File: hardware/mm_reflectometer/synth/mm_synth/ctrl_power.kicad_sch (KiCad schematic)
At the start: 60 parts

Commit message: library updates
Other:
- note added: "CHANGE TO DBVR PACKAGE"
- note added: "CHANGE TO DCKR PACKAGE"
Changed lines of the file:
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@@
     (effects (font (size 1.27 1.27)) (justify left bottom))
+  )
+  (text "CHANGE TO DBVR PACKAGE" (at 334.01 187.96 180)
+    (effects (font (size 3 3) (thickness 0.6) bold) (justify right bottom))
+  )
+  (text "CHANGE TO DCKR PACKAGE" (at 334.645 92.075 180)
+    (effects (font (size 3 3) (thickness 0.6) bold) (justify right bottom))
   )
   (label "PGOOD" (at 264.795 59.055 0)

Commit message: adding digital connections to synth schematic
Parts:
- removed C? (x4): 1uF, Capacitor_SMD:C_0402_1005Metric, symbol Device:C
- removed C? (x4): 10uF, Capacitor_SMD:C_0603_1608Metric, symbol Device:C
- removed C? (x3): 4.7uF, Capacitor_SMD:C_0402_1005Metric, symbol Device:C
- removed C? (x2): 6.8pF, Capacitor_SMD:C_0402_1005Metric, symbol Device:C
- removed R?: 10k, Resistors_SMD:R_0402, symbol Device:R_Small
- removed R?: 10k, Resistor_SMD:R_0402_1005Metric, symbol Device:R
- removed R?: 47k, Resistor_SMD:R_0402_1005Metric, symbol Device:R
- removed R?: 210k, Resistor_SMD:R_0402_1005Metric, symbol Device:R
- removed R?: 100k, Resistor_SMD:R_0402_1005Metric, symbol Device:R
- removed R?: 24k3, Resistor_SMD:R_0402_1005Metric, symbol Device:R
- removed R?: 84k5, Resistor_SMD:R_0402_1005Metric, symbol Device:R
- added C? (x7): 10 uF, Capacitors_SMD:C_0603, symbol Device:C_Small
- added C? (x4): 2.2 uF, Capacitors_SMD:C_0603, symbol Device:C_Small
- added C? (x2): 6.8 pF, symbol Device:C_Small
- added R?: 10k, Resistor_SMD:R_0402_1005Metric, symbol Device:R_Small
- added R?: 210k, symbol Device:R_Small
- added R? (x2): 10k, Resistors_SMD:R_0402, symbol Device:R_Small
- added R?: 100k, symbol Device:R_Small
- added R?: 47k, symbol Device:R_Small
- added R?: 84.5k, symbol Device:R_Small
- R? (x2): value 10k -> DNI
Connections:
- net PGOOD_5V5 is gone; now on net PGOOD_SWITCHING: U?.B4 (PGOOD2)
- net +1V1: now also C?.1, C?.1, C?.1, R?.1
- net +1V8: now also C?.1, C?.1
- net +2V5: now also C?.1, C?.1
- net +3V3: now also C?.1, C?.1, C?.1, C?.1, R?.1
- net +4V: now also R?.2; no longer C?.1, L?.1
- net +5V: now also C?.1, C?.1
- net +9V: now also C?.1, L?.1, R?.2, R?.2
- net GND: now also C?.2, C?.2, C?.2, C?.2, C?.2, C?.2, C?.2, C?.2, C?.2, C?.2, C?.2, R?.2, R?.2, R?.2
- net at U?.1 (FB): now also C?.2, R?.1, R?.2 (x2)
- net 4V0_EN: no longer names the net of R?.1, U?.D2 (RUN1)
- net 4V0_EN: now also R?.1
- net 5V5_EN: no longer names the net of R?.1, U?.B2 (RUN2)
- net 5V5_EN: now also R?.1
- net PGOOD renamed DIGITAL_SEQ_EN
- net DIGITAL_SEQ_EN: now also R?.1
- net PGOOD_4V0 renamed PGOOD_SWITCHING
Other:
- note added: "9V +/- 10% input, TBD A"
- note added: "CHANGE SERIES INDUCTOR"
- note added: "SET NEW OV/UV RESISTORS"
- note removed: "4V +/- 5% input, 1.5A"
- note removed: "TBD PULLUP ON PGOOD"
- note removed: "USB PD?"
- moved on the sheet: L?, R?, U?

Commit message: work on mm synth schematic - control signals and footprint assignments
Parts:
- removed L?: BLM18EG101TN1D, Inductor_SMD:L_0603_1608Metric, symbol Device:L_Small
- added FB?: BLM18EG101TN1D, symbol Device:FerriteBead_Small
- C1502, C1506, C1510, C1511, C1513, C1514, C1515, C1516, C1517, C1520, C1521, C1522, C1523, C1524, C1525: renamed from C?; footprint Capacitors_SMD:C_0603 -> Capacitor_SMD:C_0603_1608Metric
- C1504, C1505: renamed from C?; footprint Capacitors_SMD:C_0402 -> Capacitor_SMD:C_0402_1005Metric
- C1507, C1508: renamed from C?; footprint Capacitors_SMD:C_1210 -> Capacitor_SMD:C_1210_3225Metric
- C1518, C1519: renamed from C?; footprint (none) -> Capacitor_SMD:C_0402_1005Metric
- R1519, R1520, R1521, R1522: renamed from R?; footprint (none) -> Resistor_SMD:R_0402_1005Metric
- gave numbers to parts that had none: 33
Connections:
- net +9V: now also FB?.2
- net at C1509.1, Q1501.5 (D2), Q1501.6 (D2)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: now also FB?.1
- net ~FPGA_RESET renamed ~{FPGA_RESET}

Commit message: added aux high speed io connector, fixed hierarchical buses
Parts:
- FB1501: renamed from FB?; footprint (none) -> Inductor_SMD:L_0603_1608Metric
- R1501, R1502, R1503, R1504, R1508, R1509, R1511, R1513, R1514: footprint Resistors_SMD:R_0402 -> Resistor_SMD:R_0402_1005Metric
- renumbered L1502 to L1501, L1503 to L1502
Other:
- note added: "VERIFY SEQUENCING"
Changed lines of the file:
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@@
     (effects (font (size 1.27 1.27)) (justify left bottom))
+  )
+  (text "VERIFY SEQUENCING\n" (at 242.57 26.67 0)
+    (effects (font (size 3 3) (thickness 0.6) bold) (justify left bottom))
   )
   (text "Turn on at VBUS >4.1V" (at 279.4 69.85 0)
@@
   (symbol (lib_id "Device:L_Small") (at 308.61 148.59 90) (unit 1)
     (in_bom yes) (on_board yes)
-    (property "Reference" "L1502" (id 0) (at 308.61 143.9988 90))
+    (property "Reference" "L1501" (id 0) (at 308.61 143.9988 90))
     (property "Value" "2.2uH" (id 1) (at 308.61 146.2975 90))
     (property "Footprint" "Inductor_SMD:L_0805_2012Metric" (id 2) (at 308.61 148.59 0)
@@
   (symbol (lib_id "Device:L_Small") (at 308.61 195.58 90) (unit 1)
     (in_bom yes) (on_board yes)
-    (property "Reference" "L1503" (id 0) (at 308.61 190.9888 90))
+    (property "Reference" "L1502" (id 0) (at 308.61 190.9888 90))
     (property "Value" "2.2uH" (id 1) (at 308.61 193.2875 90))
     (property "Footprint" "Inductor_SMD:L_0805_2012Metric" (id 2) (at 308.61 195.58 0)
@@
       (effects (font (size 1.27 1.27)) (justify left))
     )
-    (property "Footprint" "Resistors_SMD:R_0402" (id 2) (at 83.82 175.26 0)
+    (property "Footprint" "Resistor_SMD:R_0402_1005Metric" (id 2) (at 83.82 175.26 0)
       (effects (font (size 1.27 1.27)) hide)
     )
@@
       (effects (font (size 1.27 1.27)) (justify left))
     )
-    (property "Footprint" "Resistors_SMD:R_0402" (id 2) (at 83.82 189.23 0)
+    (property "Footprint" "Resistor_SMD:R_0402_1005Metric" (id 2) (at 83.82 189.23 0)
       (effects (font (size 1.27 1.27)) hide)
     )
@@
       (effects (font (size 1.27 1.27)) (justify left))
     )
-    (property "Footprint" "Resistors_SMD:R_0402" (id 2) (at 90.17 175.26 0)
+    (property "Footprint" "Resistor_SMD:R_0402_1005Metric" (id 2) (at 90.17 175.26 0)
       (effects (font (size 1.27 1.27)) hide)
     )
@@
       (effects (font (size 1.27 1.27)) (justify left))
     )
-    (property "Footprint" "Resistors_SMD:R_0402" (id 2) (at 90.17 189.23 0)
+    (property "Footprint" "Resistor_SMD:R_0402_1005Metric" (id 2) (at 90.17 189.23 0)
       (effects (font (size 1.27 1.27)) hide)
     )
@@
       (effects (font (size 1.27 1.27)) (justify left))
     )
-    (property "Footprint" "Resistors_SMD:R_0402" (id 2) (at 105.41 187.96 0)
+    (property "Footprint" "Resistor_SMD:R_0402_1005Metric" (id 2) (at 105.41 187.96 0)
       (effects (font (size 1.27 1.27)) hide)
     )
@@
       (effects (font (size 1.27 1.27)) (justify left))
     )
-    (property "Footprint" "Resistors_SMD:R_0402" (id 2) (at 110.49 209.55 0)
+    (property "Footprint" "Resistor_SMD:R_0402_1005Metric" (id 2) (at 110.49 209.55 0)
       (effects (font (size 1.27 1.27)) hide)
     )
@@
       (effects (font (size 1.27 1.27)) (justify left))
     )
-    (property "Footprint" "Resistors_SMD:R_0402" (id 2) (at 128.27 134.62 0)
+    (property "Footprint" "Resistor_SMD:R_0402_1005Metric" (id 2) (at 128.27 134.62 0)
       (effects (font (size 1.27 1.27)) hide)
     )
@@
       (effects (font (size 1.27 1.27)) (justify left))
     )
-    (property "Footprint" "Resistors_SMD:R_0402" (id 2) (at 152.4 200.66 0)
+    (property "Footprint" "Resistor_SMD:R_0402_1005Metric" (id 2) (at 152.4 200.66 0)
       (effects (font (size 1.27 1.27)) hide)
     )
@@
       (effects (font (size 1.27 1.27)) (justify left))
     )
-    (property "Footprint" "Resistors_SMD:R_0402" (id 2) (at 161.29 200.66 0)
+    (property "Footprint" "Resistor_SMD:R_0402_1005Metric" (id 2) (at 161.29 200.66 0)
       (effects (font (size 1.27 1.27)) hide)
     )
@@
   (symbol (lib_id "Device:FerriteBead_Small") (at 168.91 41.91 90) (unit 1)
     (in_bom yes) (on_board yes)
-    (property "Reference" "FB?" (id 0) (at 163.83 44.45 90))
+    (property "Reference" "FB1501" (id 0) (at 163.83 44.45 90))
     (property "Value" "BLM18EG101TN1D" (id 1) (at 168.91 46.99 90))
-    (property "Footprint" "" (id 2) (at 168.91 43.688 90)
-      (effects (font (size 1.27 1.27)) hide)
-    )
+    (property "Footprint" "Inductor_SMD:L_0603_1608Metric" (id 2) (at 168.91 43.688 90)
+      (effects (font (size 1.27 1.27)) hide)
+    )

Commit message: schematic cleanup, erc
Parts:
- C1501: symbol vna_mm_ref-rescue:CP1-Device -> Device:C_Polarized_Small
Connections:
- net +4V: now also C1514.1, C1515.1, U1505.3 (VIN), U1506.3 (VIN)
- net +5V: no longer C1514.1, C1515.1, U1505.3 (VIN), U1506.3 (VIN)
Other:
- note added: "ADD INPUT POWER CONNECTFOR ADD +5V REGULATOR"
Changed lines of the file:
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@@
   (no_connect (at 149.86 179.07))
   (no_connect (at 149.86 181.61))
-  (wire (pts (xy 73.66 35.56) (xy 73.66 48.26))
-    (stroke (width 0) (type solid) (color 0 0 0 0))
-  )
-  (wire (pts (xy 73.66 55.88) (xy 73.66 58.42))
+  (wire (pts (xy 73.66 35.56) (xy 73.66 49.53))
+    (stroke (width 0) (type solid) (color 0 0 0 0))
+  )
+  (wire (pts (xy 73.66 54.61) (xy 73.66 58.42))
     (stroke (width 0) (type solid) (color 0 0 0 0))
   )
@@
   (text "SET NEW OV/UV RESISTORS" (at 31.75 73.66 0)
     (effects (font (size 3 3) (thickness 0.6) bold) (justify left bottom))
+  )
+  (text "ADD INPUT POWER CONNECTFOR\nADD +5V REGULATOR" (at 73.66 116.84 0)
+    (effects (font (size 5 5) (thickness 1) bold) (justify left bottom))
   )
   (text "9V +/- 10% input, TBD A" (at 80.01 26.67 0)
@@
     (pin "1")
   )
+  (symbol (lib_id "power:+4V") (at 278.13 148.59 0) (unit 1)
+    (in_bom yes) (on_board yes)
+    (property "Reference" "#PWR0102" (id 0) (at 278.13 152.4 0)
+      (effects (font (size 1.27 1.27)) hide)
+    )
+    (property "Value" "+4V" (id 1) (at 275.59 144.3354 0)
+      (effects (font (size 1.27 1.27)) (justify left))
+    )
+    (property "Footprint" "" (id 2) (at 278.13 148.59 0)
+      (effects (font (size 1.27 1.27)) hide)
+    )
+    (property "Datasheet" "" (id 3) (at 278.13 148.59 0)
+      (effects (font (size 1.27 1.27)) hide)
+    )
+    (pin "1")
+  )
+  (symbol (lib_id "power:+4V") (at 278.13 195.58 0) (unit 1)
+    (in_bom yes) (on_board yes)
+    (property "Reference" "#PWR0101" (id 0) (at 278.13 199.39 0)
+      (effects (font (size 1.27 1.27)) hide)
+    )
+    (property "Value" "+4V" (id 1) (at 275.59 191.3254 0)
+      (effects (font (size 1.27 1.27)) (justify left))
+    )
+    (property "Footprint" "" (id 2) (at 278.13 195.58 0)
+      (effects (font (size 1.27 1.27)) hide)
+    )
+    (property "Datasheet" "" (id 3) (at 278.13 195.58 0)
+      (effects (font (size 1.27 1.27)) hide)
+    )
+    (pin "1")
+  )
   (symbol (lib_id "power:+5V") (at 295.91 44.45 0) (unit 1)
     (in_bom yes) (on_board yes)
@@
     (pin "")
   )
-  (symbol (lib_id "gkl_power:GND") (at 313.69 173.99 0) (unit 1)
-    (in_bom yes) (on_board yes)
-    (property "Reference" "#PWR01550" (id 0) (at 313.69 180.34 0)
-      (effects (font (size 1.27 1.27)) hide)
-    )
-    (property "Value" "GND" (id 1) (at 313.7662 177.1904 0))
-    (property "Footprint" "" (id 2) (at 311.15 182.88 0)
-      (effects (font (size 1.27 1.27)) hide)
-    )
-    (property "Datasheet" "" (id 3) (at 313.69 173.99 0)
-      (effects (font (size 1.27 1.27)) hide)
-    )
-    (pin "1")
-  )
   (symbol (lib_id "Device:L_Small") (at 308.61 148.59 90) (unit 1)
     (in_bom yes) (on_board yes)
@@
     (pin "2")
   )
-  (symbol (lib_id "gkl_power:+5V") (at 278.13 148.59 0) (unit 1)
-    (in_bom yes) (on_board yes)
-    (property "Reference" "#PWR01539" (id 0) (at 278.13 152.4 0)
-      (effects (font (size 1.27 1.27)) hide)
-    )
-    (property "Value" "+5V" (id 1) (at 278.2062 144.7546 0))
-    (property "Footprint" "" (id 2) (at 278.13 148.59 0)
-      (effects (font (size 1.27 1.27)) hide)
-    )
-    (property "Datasheet" "" (id 3) (at 278.13 148.59 0)
-      (effects (font (size 1.27 1.27)) hide)
-    )
-    (pin "1")
-  )
-  (symbol (lib_id "gkl_power:+5V") (at 278.13 195.58 0) (unit 1)
-    (in_bom yes) (on_board yes)
-    (property "Reference" "#PWR01541" (id 0) (at 278.13 199.39 0)
-      (effects (font (size 1.27 1.27)) hide)
-    )
-    (property "Value" "+5V" (id 1) (at 278.2062 191.7446 0))
-    (property "Footprint" "" (id 2) (at 278.13 195.58 0)
-      (effects (font (size 1.27 1.27)) hide)
-    )
-    (property "Datasheet" "" (id 3) (at 278.13 195.58 0)
-      (effects (font (size 1.27 1.27)) hide)
-    )
-    (pin "1")
-  )
   (symbol (lib_id "power:GND") (at 73.66 58.42 0) (unit 1)
     (in_bom yes) (on_board yes)
@@
     )
     (property "Datasheet" "" (id 3) (at 307.34 115.57 0)
+      (effects (font (size 1.27 1.27)) hide)
+    )
+    (pin "1")
+  )
+  (symbol (lib_id "power:GND") (at 313.69 173.99 0) (unit 1)
+    (in_bom yes) (on_board yes)
+    (property "Reference" "#PWR0103" (id 0) (at 313.69 180.34 0)
+      (effects (font (size 1.27 1.27)) hide)
+    )
+    (property "Value" "GND" (id 1) (at 313.69 177.8 0))
+    (property "Footprint" "" (id 2) (at 313.69 173.99 0)
+      (effects (font (size 1.27 1.27)) hide)
+    )
+    (property "Datasheet" "" (id 3) (at 313.69 173.99 0)
       (effects (font (size 1.27 1.27)) hide)
     )
@@
     (pin "2")
   )
+  (symbol (lib_id "Device:C_Polarized_Small") (at 73.66 52.07 0) (unit 1)
+    (in_bom yes) (on_board yes)
+    (property "Reference" "C1501" (id 0) (at 76.581 50.9016 0)
+      (effects (font (size 1.27 1.27)) (justify left))
+    )
+    (property "Value" "330 uF" (id 1) (at 76.581 53.213 0)
+      (effects (font (size 1.27 1.27)) (justify left))
+    )
+    (property "Footprint" "Capacitor_SMD:CP_Elec_6.3x5.9" (id 2) (at 73.66 52.07 0)
+      (effects (font (size 1.27 1.27)) hide)
+    )
+    (property "Datasheet" "~" (id 3) (at 73.66 52.07 0)
+      (effects (font (size 1.27 1.27)) hide)
+    )
+    (property "MAN_NAME" "Panasonic" (id 4) (at 73.66 52.07 0)
+      (effects (font (size 1.27 1.27)) hide)
+    )
+    (property "MAN_PN" "6SVPC330M" (id 5) (at 73.66 52.07 0)
+      (effects (font (size 1.27 1.27)) hide)
+    )
+    (property "DIST_NAME" "Digi-Key" (id 6) (at 73.66 52.07 0)
+      (effects (font (size 1.27 1.27)) hide)
+    )
+    (property "DIST_PN" "P16611CT-ND" (id 7) (at 73.66 52.07 0)
+      (effects (font (size 1.27 1.27)) hide)
+    )
+    (pin "1")
+    (pin "2")
+  )
   (symbol (lib_id "Device:C_Small") (at 87.63 153.67 0) (unit 1)
     (in_bom yes) (on_board yes)
@@
       (effects (font (size 1.27 1.27)) hide)
     )
-    (pin "1")
-    (pin "2")
-  )
-  (symbol (lib_id "vna_mm_ref-rescue:CP1-Device") (at 73.66 52.07 0) (unit 1)
-    (in_bom yes) (on_board yes)
-    (property "Reference" "C1501" (id 0) (at 76.581 50.9016 0)
-      (effects (font (size 1.27 1.27)) (justify left))
-    )
-    (property "Value" "330 uF" (id 1) (at 76.581 53.213 0)
-      (effects (font (size 1.27 1.27)) (justify left))
-    )
-    (property "Footprint" "Capacitor_SMD:CP_Elec_6.3x5.9" (id 2) (at 73.66 52.07 0)
-      (effects (font (size 1.27 1.27)) hide)
-    )
-    (property "Datasheet" "~" (id 3) (at 73.66 52.07 0)
-      (effects (font (size 1.27 1.27)) hide)
-    )
-    (property "MAN_NAME" "Panasonic" (id 4) (at 73.66 52.07 0)
-      (effects (font (size 1.27 1.27)) hide)
-    )
-    (property "MAN_PN" "6SVPC330M" (id 5) (at 73.66 52.07 0)
-      (effects (font (size 1.27 1.27)) hide)
-    )
-    (property "DIST_NAME" "Digi-Key" (id 6) (at 73.66 52.07 0)
-      (effects (font (size 1.27 1.27)) hide)
-    )
-    (property "DIST_PN" "P16611CT-ND" (id 7) (at 73.66 52.07 0)
-      (effects (font (size 1.27 1.27)) hide)
-    )

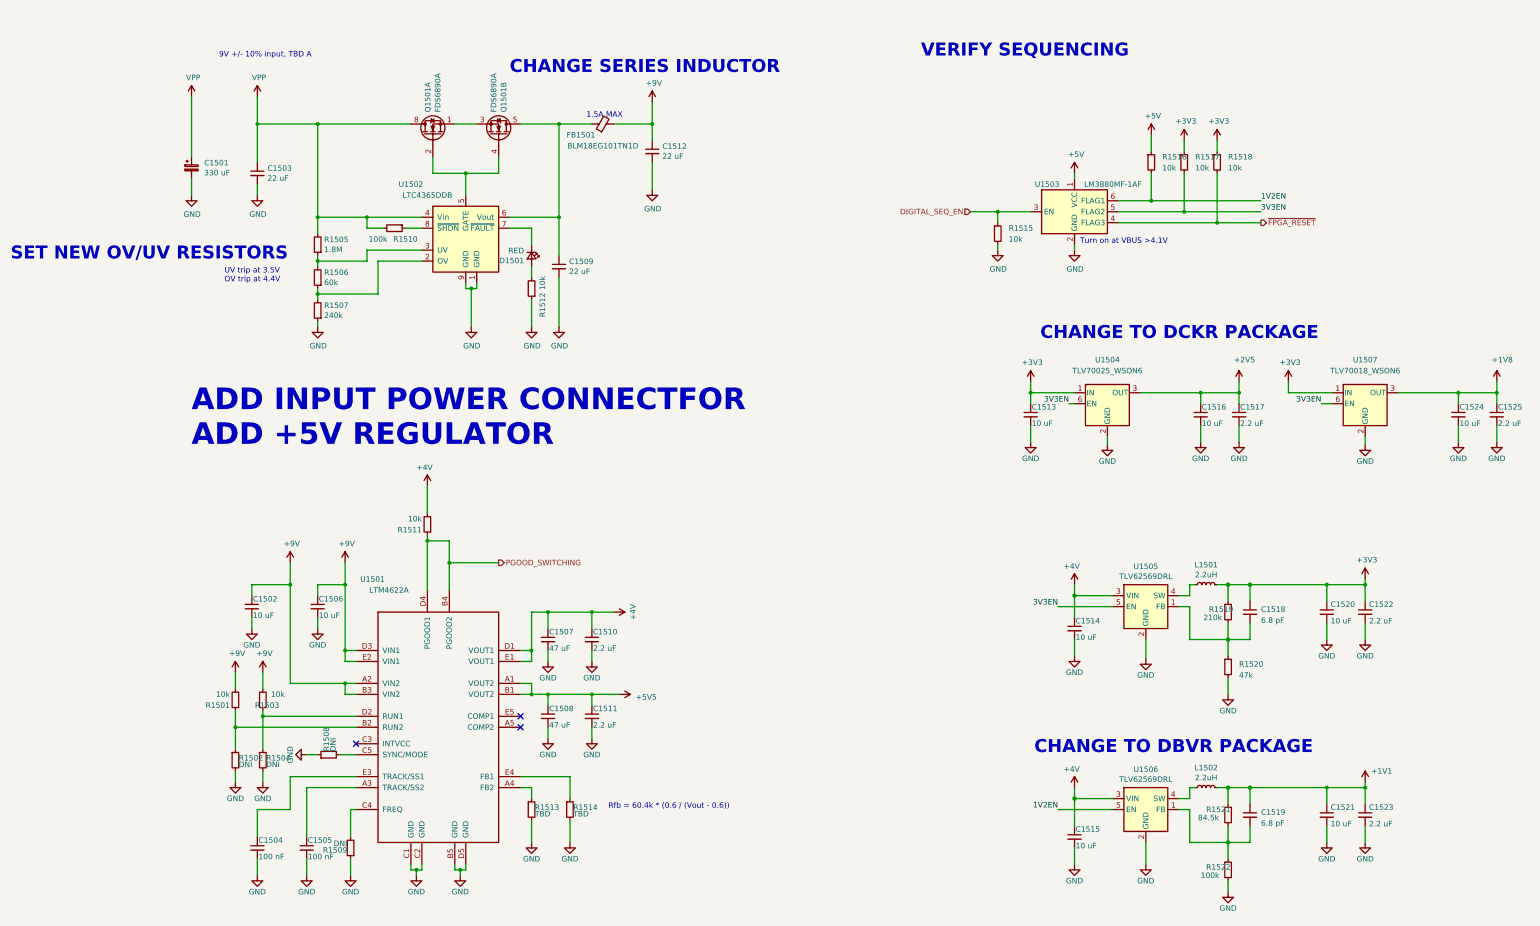
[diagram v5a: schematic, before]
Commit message: added usb PD sink to synth
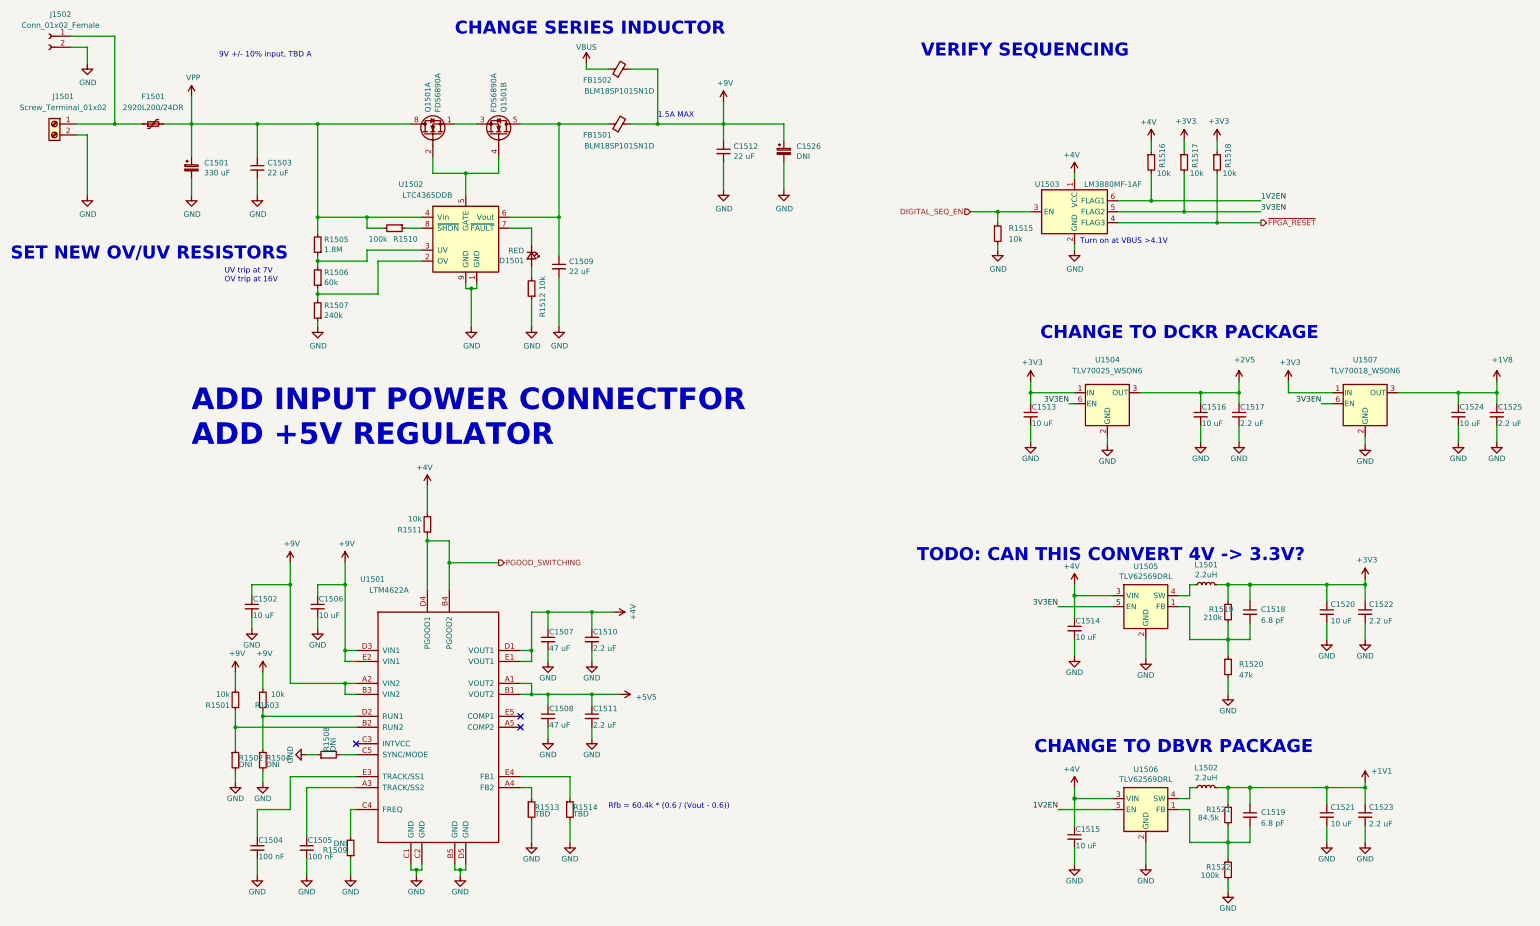
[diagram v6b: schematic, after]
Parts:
- added C1526: DNI, Capacitor_SMD:CP_Elec_6.3x5.9, symbol Device:C_Polarized_Small
- added F1501: 2920L200/24DR, Fuse:Fuse_2920_7451Metric, symbol Device:Polyfuse_Small
- added FB1502: BLM18SP101SN1D, Inductor_SMD:L_0603_1608Metric, symbol Device:FerriteBead_Small
- added J1501: Screw_Terminal_01x02, TerminalBlock_Phoenix:TerminalBlock_Phoenix_MPT-0,5-2-2.54_1x02_P2.54mm_Horizontal, symbol Connector:Screw_Terminal_01x02
- added J1502: Conn_01x02_Female, Connector_Molex:Molex_Nano-Fit_105309-xx02_1x02_P2.50mm_Vertical, symbol Connector:Conn_01x02_Female
- FB1501: value BLM18EG101TN1D -> BLM18SP101SN1D
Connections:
- net +5V is gone; now on net +4V: R1516.1, U1503.1 (VCC)
- net +9V: now also C1526.1, FB1502.2
- net GND: now also C1526.2, J1501.2 (Pin_2), J1502.2 (Pin_2)
- net VPP: now also F1501.2
- new net: F1501.1, J1501.1 (Pin_1), J1502.1 (Pin_1)
- new net VBUS: FB1502.1
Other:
- note added: "TODO: CAN THIS CONVERT 4V -> 3.3V?"
- note added: "UV trip at 7V OV trip at 16V"
- note removed: "UV trip at 3.5V OV trip at 4.4V"
- moved on the sheet: C1503, C1512, FB1501
